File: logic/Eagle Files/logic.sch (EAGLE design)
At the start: 62 parts, among them J1 Under Glow, J2 B2PS-VH(LF)(SN), J3 B2PS-VH(LF)(SN), J4 B2PS-VH(LF)(SN), J5 B2PS-VH(LF)(SN), J6 B2PS-VH(LF)(SN), Q4 STT4P3LLH6, Q5 RRH100P03GZETB, T1 R-78E5.0-1.0, U1 9DoF IMU, U4 TLV70233DBVR, U5 TC4427ACOA713, U6 TC4427ACOA713, U7 TC4427ACOA713, X1 MINI-USB_SHIELD5P4-32005-400, X2 C-GRID-05-15-91, X3 2510-, X4 2510-, X5 C-GRID-05-15-91, X6 C-GRID-02-70553, X7 SI-50170

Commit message: added various components
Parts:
- added C11: 0.1uF, rcl:C-USC0603
- added C12: 1nF, rcl:C-USC0603
- added R2: 1k, rcl:R-US_R0603
- added U$17: ACS711, IGVC-Sensor:ACS711
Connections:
- new net N$3: C12.1, U$17.VIOUT
- new net N$4: R2.1, U$17.!FAULT
- new net N$5: U$17.IP+
- new net N$6: U$17.IP-
- net +3V3: now also C11.1, R2.2, U$17.VCC
- net GND: now also C11.2, C12.2, U$17.GND
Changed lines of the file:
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@@
 <?xml version="1.0" encoding="utf-8"?>
 <!DOCTYPE eagle SYSTEM "eagle.dtd">
-<eagle version="8.7.0">
+<eagle version="9.1.3">
 <drawing>
 <settings>
@@
 <part name="J6" library="RoboJackets-Connectors" deviceset="B2P?-VH(LF)(SN)" device="S"/>
 <part name="GND16" library="supply1" deviceset="GND" device=""/>
+<part name="FRAME5" library="RoboJackets-Frames" deviceset="FRAME_A_L" device=""/>
+<part name="FRAME6" library="RoboJackets-Frames" deviceset="FRAME_A_L" device=""/>
+<part name="U$17" library="IGVC-Sensor" deviceset="ACS711" device=""/>
+<part name="+3V1" library="supply1" library_urn="urn:adsk.eagle:library:371" deviceset="+3V3" device=""/>
+<part name="C11" library="rcl" library_urn="urn:adsk.eagle:library:334" deviceset="C-US" device="C0603" package3d_urn="urn:adsk.eagle:package:23616/2" value="0.1uF"/>
+<part name="GND17" library="supply1" library_urn="urn:adsk.eagle:library:371" deviceset="GND" device=""/>
+<part name="C12" library="rcl" library_urn="urn:adsk.eagle:library:334" deviceset="C-US" device="C0603" package3d_urn="urn:adsk.eagle:package:23616/2" value="1nF"/>
+<part name="GND19" library="supply1" library_urn="urn:adsk.eagle:library:371" deviceset="GND" device=""/>
+<part name="R2" library="rcl" library_urn="urn:adsk.eagle:library:334" deviceset="R-US_" device="R0603" package3d_urn="urn:adsk.eagle:package:23555/2" value="1k"/>
+<part name="GND20" library="supply1" library_urn="urn:adsk.eagle:library:371" deviceset="GND" device=""/>
 </parts>
 <sheets>
@@
 </sheet>
 <sheet>
-<description>Misc. Power and Headers</description>
+<description>Power Distribution</description>
+<plain>
+</plain>
+<instances>
+<instance part="FRAME5" gate="G$1" x="0" y="0"/>
+<instance part="FRAME6" gate="G$2" x="172.72" y="0"/>
+<instance part="U$17" gate="G$1" x="200.66" y="147.32"/>
+<instance part="+3V1" gate="G$1" x="236.22" y="195.58"/>
+<instance part="C11" gate="G$1" x="248.92" y="182.88"/>
+<instance part="GND17" gate="1" x="248.92" y="172.72"/>
+<instance part="C12" gate="G$1" x="251.46" y="160.02"/>
+<instance part="GND19" gate="1" x="251.46" y="149.86"/>
+<instance part="R2" gate="G$1" x="241.3" y="175.26" rot="R90"/>
+<instance part="GND20" gate="1" x="228.6" y="144.78"/>
+</instances>
+<busses>
+</busses>
+<nets>
+<net name="+3V3" class="0">
+<segment>
+<pinref part="U$17" gate="G$1" pin="VCC"/>
+<pinref part="+3V1" gate="G$1" pin="+3V3"/>
+<wire x1="225.66" y1="172.32" x2="236.22" y2="172.32" width="0.1524" layer="91"/>
+<wire x1="236.22" y1="172.32" x2="236.22" y2="187.96" width="0.1524" layer="91"/>
+<pinref part="C11" gate="G$1" pin="1"/>
+<wire x1="236.22" y1="187.96" x2="236.22" y2="193.04" width="0.1524" layer="91"/>
+<wire x1="248.92" y1="185.42" x2="248.92" y2="187.96" width="0.1524" layer="91"/>
+<wire x1="248.92" y1="187.96" x2="241.3" y2="187.96" width="0.1524" layer="91"/>
+<junction x="236.22" y="187.96"/>
+<pinref part="R2" gate="G$1" pin="2"/>
+<wire x1="241.3" y1="187.96" x2="236.22" y2="187.96" width="0.1524" layer="91"/>
+<wire x1="241.3" y1="180.34" x2="241.3" y2="187.96" width="0.1524" layer="91"/>
+<junction x="241.3" y="187.96"/>
+</segment>
+</net>
+<net name="GND" class="0">
+<segment>
+<pinref part="C11" gate="G$1" pin="2"/>
+<pinref part="GND17" gate="1" pin="GND"/>
+<wire x1="248.92" y1="177.8" x2="248.92" y2="175.26" width="0.1524" layer="91"/>
+</segment>
+<segment>
+<pinref part="C12" gate="G$1" pin="2"/>
+<pinref part="GND19" gate="1" pin="GND"/>
+<wire x1="251.46" y1="154.94" x2="251.46" y2="152.4" width="0.1524" layer="91"/>
+</segment>
+<segment>
+<pinref part="U$17" gate="G$1" pin="GND"/>
+<pinref part="GND20" gate="1" pin="GND"/>
+<wire x1="225.66" y1="149.82" x2="228.6" y2="149.82" width="0.1524" layer="91"/>
+<wire x1="228.6" y1="149.82" x2="228.6" y2="147.32" width="0.1524" layer="91"/>
+</segment>
+</net>
+<net name="N$3" class="0">
+<segment>
+<pinref part="C12" gate="G$1" pin="1"/>
+<pinref part="U$17" gate="G$1" pin="VIOUT"/>
+<wire x1="251.46" y1="162.56" x2="251.46" y2="164.82" width="0.1524" layer="91"/>
+<wire x1="251.46" y1="164.82" x2="225.66" y2="164.82" width="0.1524" layer="91"/>
+</segment>
+</net>
+<net name="N$4" class="0">
+<segment>
+<pinref part="U$17" gate="G$1" pin="!FAULT"/>
+<pinref part="R2" gate="G$1" pin="1"/>
+<wire x1="225.66" y1="157.32" x2="241.3" y2="157.32" width="0.1524" layer="91"/>
+<wire x1="241.3" y1="157.32" x2="241.3" y2="170.18" width="0.1524" layer="91"/>
+</segment>
+</net>
+<net name="N$5" class="0">
+<segment>
+<pinref part="U$17" gate="G$1" pin="IP+"/>
+<wire x1="195.66" y1="167.32" x2="180.34" y2="167.32" width="0.1524" layer="91"/>
+</segment>
+</net>
+<net name="N$6" class="0">
+<segment>
+<pinref part="U$17" gate="G$1" pin="IP-"/>
+<wire x1="195.66" y1="154.82" x2="195.66" y2="154.94" width="0.1524" layer="91"/>
+<wire x1="195.66" y1="154.94" x2="180.34" y2="154.94" width="0.1524" layer="91"/>
+</segment>
+</net>
+</nets>
+</sheet>
+<sheet>
+<description>Misc.</description>
 <plain>
 <wire x1="7.62" y1="208.28" x2="101.6" y2="208.28" width="0.1524" layer="103" style="shortdash"/>
@@
 packages will not be understood (or retained) with this version.
 </note>
+<note version="8.4" severity="warning">
+Since Version 8.4, EAGLE supports properties for SPICE simulation.
+Probes in schematics and SPICE mapping objects found in parts and library devices
+will not be understood with this version. Update EAGLE to the latest version
+for full support of SPICE simulation.
+</note>
 </compatibility>

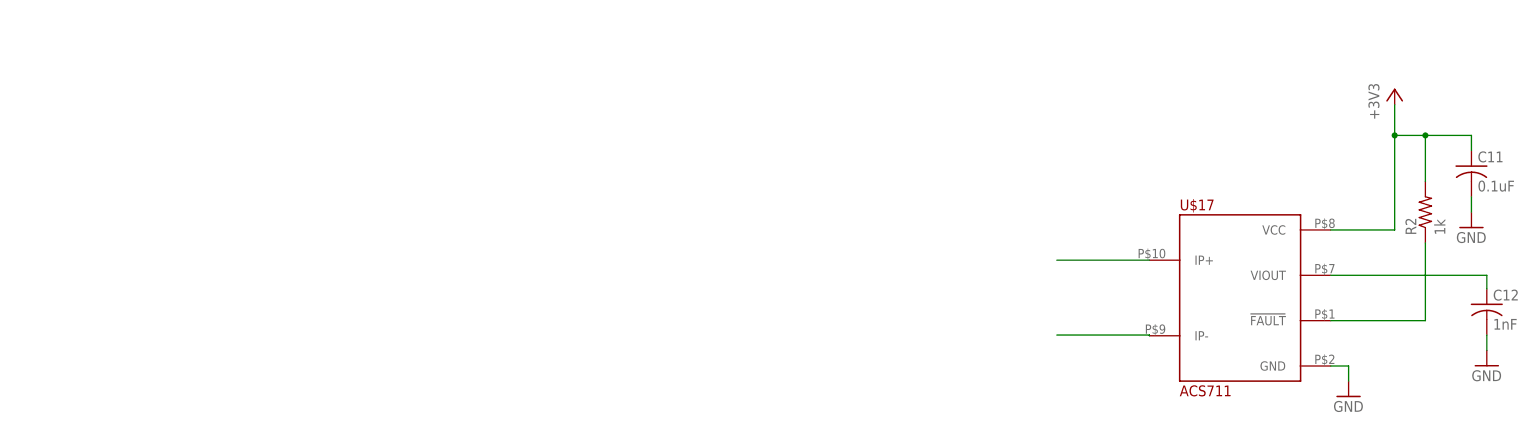
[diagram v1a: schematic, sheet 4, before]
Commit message: added safety light power
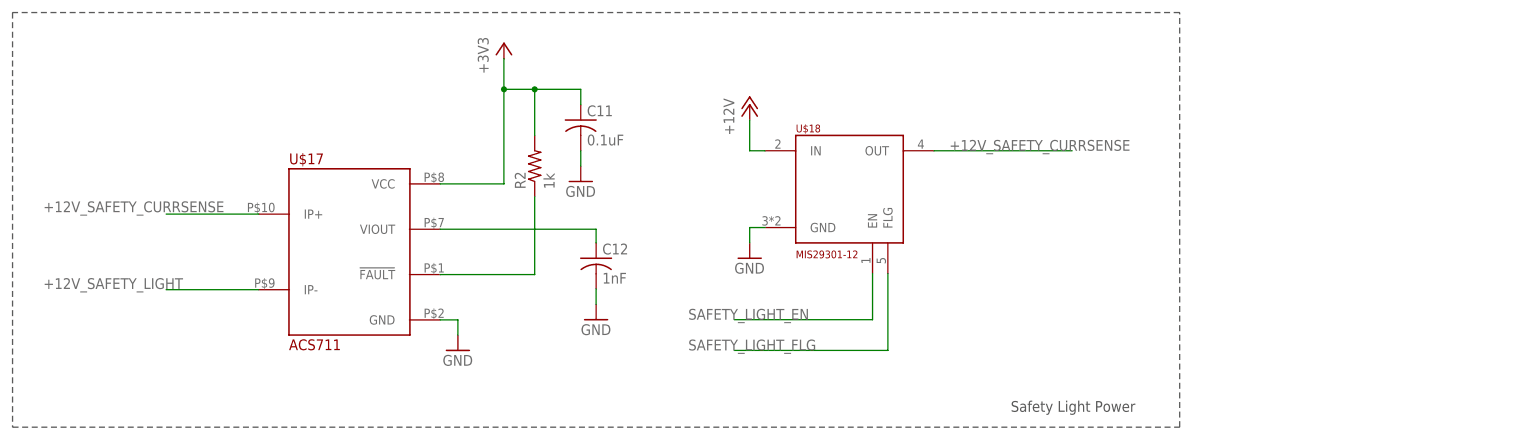
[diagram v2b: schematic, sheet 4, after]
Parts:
- added U$18: MIS29301-12, IGVC-Regulator:MIS29301-12
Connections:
- net N$6 renamed +12V_SAFETY_LIGHT
- removed net N$5: U$17.IP+
- new net +12V_SAFETY_CURRSENSE: U$17.IP+, U$18.OUT
- new net SAFETY_LIGHT_EN: U$18.EN
- new net SAFETY_LIGHT_FLG: U$18.FLG
- net +12V: now also U$18.IN
- net GND: now also U$18.GND
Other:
- note added: "Safety Light Power"
- moved on the sheet: C11, C12, R2, U$17
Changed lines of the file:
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@@
 <part name="R2" library="rcl" library_urn="urn:adsk.eagle:library:334" deviceset="R-US_" device="R0603" package3d_urn="urn:adsk.eagle:package:23555/2" value="1k"/>
 <part name="GND20" library="supply1" library_urn="urn:adsk.eagle:library:371" deviceset="GND" device=""/>
+<part name="U$18" library="IGVC-Regulator" deviceset="MIS29301-12" device=""/>
+<part name="GND34" library="supply1" library_urn="urn:adsk.eagle:library:371" deviceset="GND" device=""/>
+<part name="P+9" library="supply1" library_urn="urn:adsk.eagle:library:371" deviceset="+12V" device=""/>
 </parts>
 <sheets>
@@
 <description>Power Distribution</description>
 <plain>
+<wire x1="7.62" y1="208.28" x2="7.62" y2="139.7" width="0.1524" layer="97" style="shortdash"/>
+<wire x1="7.62" y1="139.7" x2="200.66" y2="139.7" width="0.1524" layer="97" style="shortdash"/>
+<wire x1="200.66" y1="139.7" x2="200.66" y2="208.28" width="0.1524" layer="97" style="shortdash"/>
+<wire x1="200.66" y1="208.28" x2="7.62" y2="208.28" width="0.1524" layer="97" style="shortdash"/>
+<text x="172.72" y="142.24" size="1.778" layer="97" font="vector">Safety Light Power</text>
 </plain>
 <instances>
 <instance part="FRAME5" gate="G$1" x="0" y="0"/>
 <instance part="FRAME6" gate="G$2" x="172.72" y="0"/>
-<instance part="U$17" gate="G$1" x="200.66" y="147.32"/>
-<instance part="+3V1" gate="G$1" x="236.22" y="195.58"/>
-<instance part="C11" gate="G$1" x="248.92" y="182.88"/>
-<instance part="GND17" gate="1" x="248.92" y="172.72"/>
-<instance part="C12" gate="G$1" x="251.46" y="160.02"/>
-<instance part="GND19" gate="1" x="251.46" y="149.86"/>
-<instance part="R2" gate="G$1" x="241.3" y="175.26" rot="R90"/>
-<instance part="GND20" gate="1" x="228.6" y="144.78"/>
+<instance part="U$17" gate="G$1" x="53.34" y="154.94"/>
+<instance part="+3V1" gate="G$1" x="88.9" y="203.2"/>
+<instance part="C11" gate="G$1" x="101.6" y="190.5"/>
+<instance part="GND17" gate="1" x="101.6" y="180.34"/>
+<instance part="C12" gate="G$1" x="104.14" y="167.64"/>
+<instance part="GND19" gate="1" x="104.14" y="157.48"/>
+<instance part="R2" gate="G$1" x="93.98" y="182.88" rot="R90"/>
+<instance part="GND20" gate="1" x="81.28" y="152.4"/>
+<instance part="U$18" gate="G$1" x="137.16" y="170.18"/>
+<instance part="GND34" gate="1" x="129.54" y="167.64"/>
+<instance part="P+9" gate="1" x="129.54" y="193.04"/>
 </instances>
 <busses>
@@
 <pinref part="U$17" gate="G$1" pin="VCC"/>
 <pinref part="+3V1" gate="G$1" pin="+3V3"/>
-<wire x1="225.66" y1="172.32" x2="236.22" y2="172.32" width="0.1524" layer="91"/>
-<wire x1="236.22" y1="172.32" x2="236.22" y2="187.96" width="0.1524" layer="91"/>
+<wire x1="78.34" y1="179.94" x2="88.9" y2="179.94" width="0.1524" layer="91"/>
+<wire x1="88.9" y1="179.94" x2="88.9" y2="195.58" width="0.1524" layer="91"/>
 <pinref part="C11" gate="G$1" pin="1"/>
-<wire x1="236.22" y1="187.96" x2="236.22" y2="193.04" width="0.1524" layer="91"/>
-<wire x1="248.92" y1="185.42" x2="248.92" y2="187.96" width="0.1524" layer="91"/>
-<wire x1="248.92" y1="187.96" x2="241.3" y2="187.96" width="0.1524" layer="91"/>
-<junction x="236.22" y="187.96"/>
+<wire x1="88.9" y1="195.58" x2="88.9" y2="200.66" width="0.1524" layer="91"/>
+<wire x1="101.6" y1="193.04" x2="101.6" y2="195.58" width="0.1524" layer="91"/>
+<wire x1="101.6" y1="195.58" x2="93.98" y2="195.58" width="0.1524" layer="91"/>
+<junction x="88.9" y="195.58"/>
 <pinref part="R2" gate="G$1" pin="2"/>
-<wire x1="241.3" y1="187.96" x2="236.22" y2="187.96" width="0.1524" layer="91"/>
-<wire x1="241.3" y1="180.34" x2="241.3" y2="187.96" width="0.1524" layer="91"/>
-<junction x="241.3" y="187.96"/>
+<wire x1="93.98" y1="195.58" x2="88.9" y2="195.58" width="0.1524" layer="91"/>
+<wire x1="93.98" y1="187.96" x2="93.98" y2="195.58" width="0.1524" layer="91"/>
+<junction x="93.98" y="195.58"/>
 </segment>
 </net>
@@
 <pinref part="C11" gate="G$1" pin="2"/>
 <pinref part="GND17" gate="1" pin="GND"/>
-<wire x1="248.92" y1="177.8" x2="248.92" y2="175.26" width="0.1524" layer="91"/>
+<wire x1="101.6" y1="185.42" x2="101.6" y2="182.88" width="0.1524" layer="91"/>
 </segment>
 <segment>
 <pinref part="C12" gate="G$1" pin="2"/>
 <pinref part="GND19" gate="1" pin="GND"/>
-<wire x1="251.46" y1="154.94" x2="251.46" y2="152.4" width="0.1524" layer="91"/>
+<wire x1="104.14" y1="162.56" x2="104.14" y2="160.02" width="0.1524" layer="91"/>
 </segment>
 <segment>
 <pinref part="U$17" gate="G$1" pin="GND"/>
 <pinref part="GND20" gate="1" pin="GND"/>
-<wire x1="225.66" y1="149.82" x2="228.6" y2="149.82" width="0.1524" layer="91"/>
-<wire x1="228.6" y1="149.82" x2="228.6" y2="147.32" width="0.1524" layer="91"/>
+<wire x1="78.34" y1="157.44" x2="81.28" y2="157.44" width="0.1524" layer="91"/>
+<wire x1="81.28" y1="157.44" x2="81.28" y2="154.94" width="0.1524" layer="91"/>
+</segment>
+<segment>
+<pinref part="U$18" gate="G$1" pin="GND"/>
+<pinref part="GND34" gate="1" pin="GND"/>
+<wire x1="132.08" y1="172.72" x2="129.54" y2="172.72" width="0.1524" layer="91"/>
+<wire x1="129.54" y1="172.72" x2="129.54" y2="170.18" width="0.1524" layer="91"/>
 </segment>
 </net>
@@
 <pinref part="C12" gate="G$1" pin="1"/>
 <pinref part="U$17" gate="G$1" pin="VIOUT"/>
-<wire x1="251.46" y1="162.56" x2="251.46" y2="164.82" width="0.1524" layer="91"/>
-<wire x1="251.46" y1="164.82" x2="225.66" y2="164.82" width="0.1524" layer="91"/>
+<wire x1="104.14" y1="170.18" x2="104.14" y2="172.44" width="0.1524" layer="91"/>
+<wire x1="104.14" y1="172.44" x2="78.34" y2="172.44" width="0.1524" layer="91"/>
 </segment>
 </net>
@@
 <pinref part="U$17" gate="G$1" pin="!FAULT"/>
 <pinref part="R2" gate="G$1" pin="1"/>
-<wire x1="225.66" y1="157.32" x2="241.3" y2="157.32" width="0.1524" layer="91"/>
-<wire x1="241.3" y1="157.32" x2="241.3" y2="170.18" width="0.1524" layer="91"/>
-</segment>
-</net>
-<net name="N$5" class="0">
+<wire x1="78.34" y1="164.94" x2="93.98" y2="164.94" width="0.1524" layer="91"/>
+<wire x1="93.98" y1="164.94" x2="93.98" y2="177.8" width="0.1524" layer="91"/>
+</segment>
+</net>
+<net name="+12V_SAFETY_LIGHT" class="0">
+<segment>
+<pinref part="U$17" gate="G$1" pin="IP-"/>
+<wire x1="48.34" y1="162.44" x2="33.02" y2="162.44" width="0.1524" layer="91"/>
+<label x="12.7" y="162.56" size="1.778" layer="95"/>
+</segment>
+</net>
+<net name="+12V_SAFETY_CURRSENSE" class="0">
+<segment>
+<pinref part="U$18" gate="G$1" pin="OUT"/>
+<wire x1="160.02" y1="185.42" x2="182.88" y2="185.42" width="0.1524" layer="91"/>
+<label x="162.56" y="185.42" size="1.778" layer="95"/>
+</segment>
 <segment>
 <pinref part="U$17" gate="G$1" pin="IP+"/>
-<wire x1="195.66" y1="167.32" x2="180.34" y2="167.32" width="0.1524" layer="91"/>
-</segment>
-</net>
-<net name="N$6" class="0">
-<segment>
-<pinref part="U$17" gate="G$1" pin="IP-"/>
-<wire x1="195.66" y1="154.82" x2="195.66" y2="154.94" width="0.1524" layer="91"/>
-<wire x1="195.66" y1="154.94" x2="180.34" y2="154.94" width="0.1524" layer="91"/>
-</segment>
-</net>
+<wire x1="48.34" y1="174.94" x2="33.02" y2="174.94" width="0.1524" layer="91"/>
+<label x="12.7" y="175.26" size="1.778" layer="95"/>
+</segment>
+</net>
+<net name="+12V" class="0">
+<segment>
+<pinref part="U$18" gate="G$1" pin="IN"/>
+<pinref part="P+9" gate="1" pin="+12V"/>
+<wire x1="132.08" y1="185.42" x2="129.54" y2="185.42" width="0.1524" layer="91"/>
+<wire x1="129.54" y1="185.42" x2="129.54" y2="190.5" width="0.1524" layer="91"/>
+</segment>
+</net>
+<net name="SAFETY_LIGHT_EN" class="0">
+<segment>
+<pinref part="U$18" gate="G$1" pin="EN"/>
+<wire x1="149.86" y1="165.1" x2="149.86" y2="157.48" width="0.1524" layer="91"/>
+<wire x1="149.86" y1="157.48" x2="127" y2="157.48" width="0.1524" layer="91"/>
+<label x="119.38" y="157.48" size="1.778" layer="95"/>
+</segment>
+</net>
+<net name="SAFETY_LIGHT_FLG" class="0">
+<segment>
+<pinref part="U$18" gate="G$1" pin="FLG"/>
+<wire x1="152.4" y1="165.1" x2="152.4" y2="152.4" width="0.1524" layer="91"/>
+<wire x1="152.4" y1="152.4" x2="127" y2="152.4" width="0.1524" layer="91"/>
+<label x="119.38" y="152.4" size="1.778" layer="95"/>
+</segment>
+</net>

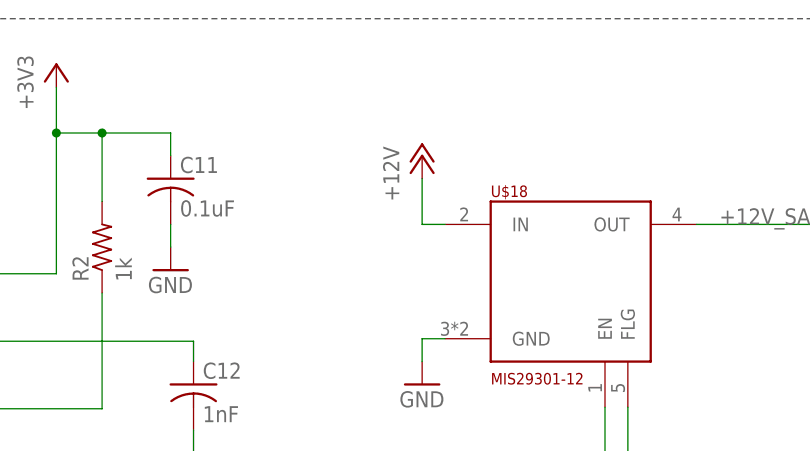
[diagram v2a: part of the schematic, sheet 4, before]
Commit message: fixed +24V to safety regulator
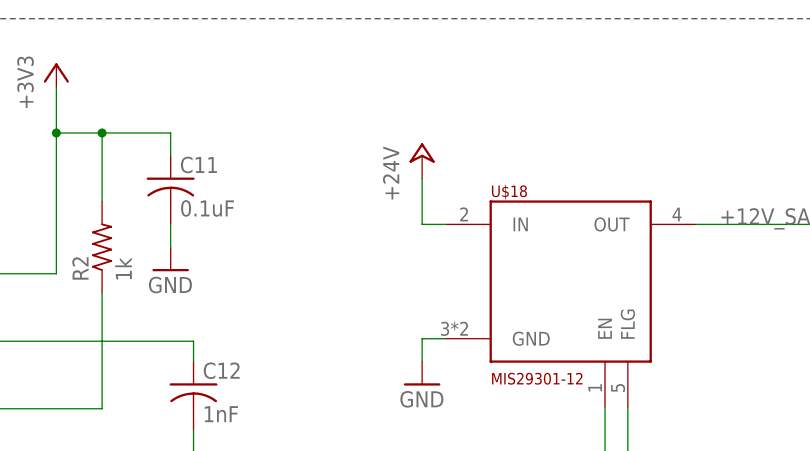
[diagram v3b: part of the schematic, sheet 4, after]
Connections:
- net +12V: no longer U$18.IN
- net +24V: now also U$18.IN
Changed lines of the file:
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@@
 <part name="U$18" library="IGVC-Regulator" deviceset="MIS29301-12" device=""/>
 <part name="GND34" library="supply1" library_urn="urn:adsk.eagle:library:371" deviceset="GND" device=""/>
-<part name="P+9" library="supply1" library_urn="urn:adsk.eagle:library:371" deviceset="+12V" device=""/>
+<part name="P+9" library="supply1" library_urn="urn:adsk.eagle:library:371" deviceset="+24V" device=""/>
 </parts>
 <sheets>
@@
 </segment>
 </net>
-<net name="+12V" class="0">
-<segment>
-<pinref part="U$18" gate="G$1" pin="IN"/>
-<pinref part="P+9" gate="1" pin="+12V"/>
-<wire x1="132.08" y1="185.42" x2="129.54" y2="185.42" width="0.1524" layer="91"/>
-<wire x1="129.54" y1="185.42" x2="129.54" y2="190.5" width="0.1524" layer="91"/>
-</segment>
-</net>
 <net name="SAFETY_LIGHT_EN" class="0">
 <segment>
@@
 </segment>
 </net>
+<net name="+24V" class="0">
+<segment>
+<pinref part="U$18" gate="G$1" pin="IN"/>
+<wire x1="132.08" y1="185.42" x2="129.54" y2="185.42" width="0.1524" layer="91"/>
+<wire x1="129.54" y1="185.42" x2="129.54" y2="190.5" width="0.1524" layer="91"/>
+<pinref part="P+9" gate="1" pin="+24V"/>
+</segment>
+</net>
